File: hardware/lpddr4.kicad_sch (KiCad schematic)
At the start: 64 parts, among them IC11 K4F6E3S4HM-MGCJ, IC12 K4F6E3S4HM-MGCJ, U9 MPFS025T-FCVG484E

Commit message: assigned footprints of resistors and some capacitors
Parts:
- C101, C126, C127, C150, C151: value C -> 10uF; footprint (none) -> payload_footprints:CAPC1608X100N
- R105: value R_US -> 240R; footprint (none) -> payload_footprints:RESC1005X40N
- R106: value R_US -> 10K; footprint (none) -> payload_footprints:RC0402N_YAG
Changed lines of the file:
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@@
 			)
 		)
-		(property "Value" "C"
+		(property "Value" "10uF"
 			(at 202.946 266.446 0)
 			(show_name no)
@@
 			)
 		)
-		(property "Footprint" ""
+		(property "Footprint" "payload_footprints:CAPC1608X100N"
 			(at 200.9648 260.35 0)
 			(hide yes)
@@
 			)
 		)
-		(property "Value" "R_US"
+		(property "Value" "10K"
 			(at 255.905 181.6099 0)
 			(show_name no)
@@
 			)
 		)
-		(property "Footprint" ""
+		(property "Footprint" "payload_footprints:RC0402N_YAG"
 			(at 252.984 180.086 90)
 			(hide yes)
@@
 			)
 		)
-		(property "Value" "R_US"
+		(property "Value" "240R"
 			(at 265.43 158.242 90)
 			(show_name no)
@@
 			)
 		)
-		(property "Footprint" ""
+		(property "Footprint" "payload_footprints:RESC1005X40N"
 			(at 259.334 159.004 90)
 			(hide yes)
@@
 			)
 		)
-		(property "Value" "C"
+		(property "Value" "10uF"
 			(at 210.566 235.966 0)
 			(show_name no)
@@
 			)
 		)
-		(property "Footprint" ""
+		(property "Footprint" "payload_footprints:CAPC1608X100N"
 			(at 208.5848 229.87 0)
 			(hide yes)
@@
 			)
 		)
-		(property "Value" "C"
+		(property "Value" "10uF"
 			(at 195.326 266.446 0)
 			(show_name no)
@@
 			)
 		)
-		(property "Footprint" ""
+		(property "Footprint" "payload_footprints:CAPC1608X100N"
 			(at 193.3448 260.35 0)
 			(hide yes)
@@
 			)
 		)
-		(property "Value" "C"
+		(property "Value" "10uF"
 			(at 216.916 206.756 0)
 			(show_name no)
@@
 			)
 		)
-		(property "Footprint" ""
+		(property "Footprint" "payload_footprints:CAPC1608X100N"
 			(at 214.9348 200.66 0)
 			(hide yes)
@@
 			)
 		)
-		(property "Value" "C"
+		(property "Value" "10uF"
 			(at 218.186 235.966 0)
 			(show_name no)
@@
 			)
 		)
-		(property "Footprint" ""
+		(property "Footprint" "payload_footprints:CAPC1608X100N"
 			(at 216.2048 229.87 0)
 			(hide yes)

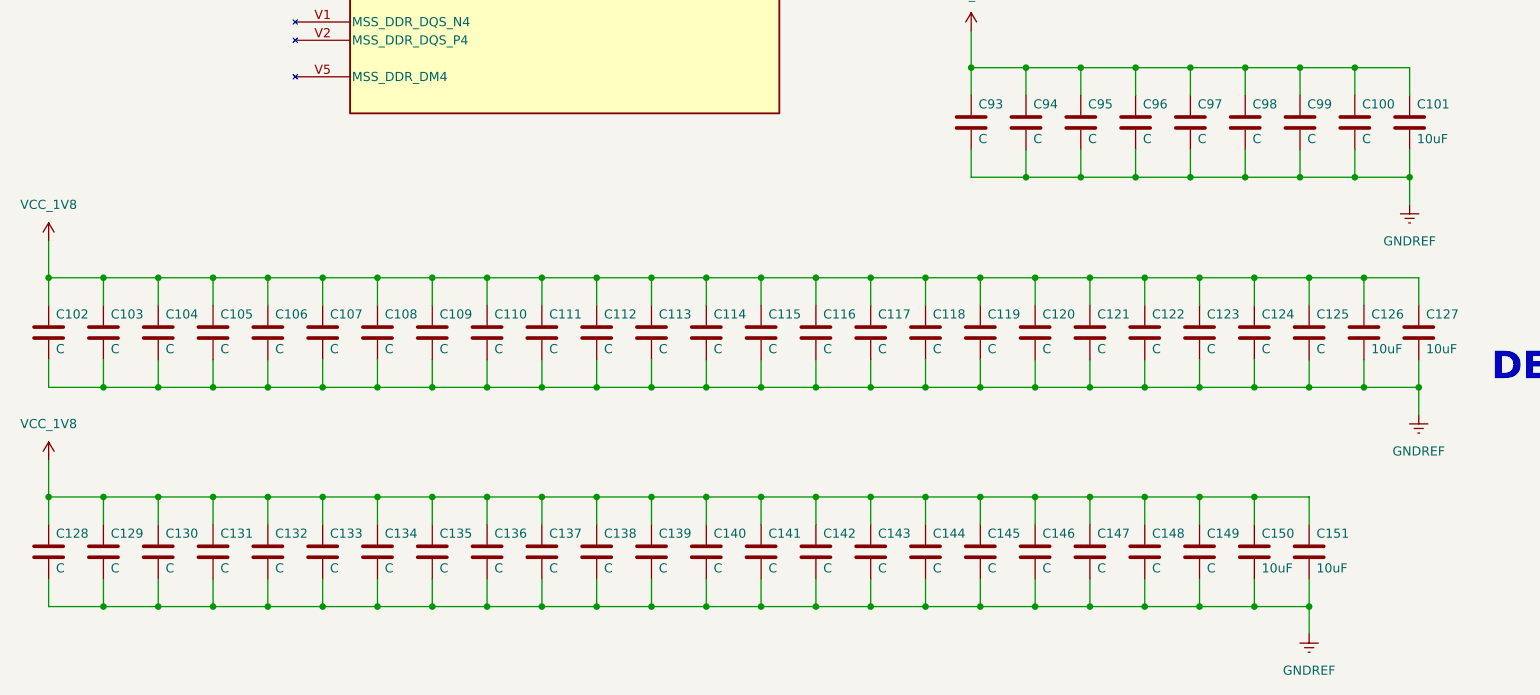
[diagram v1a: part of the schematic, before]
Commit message: added capacitors footprints
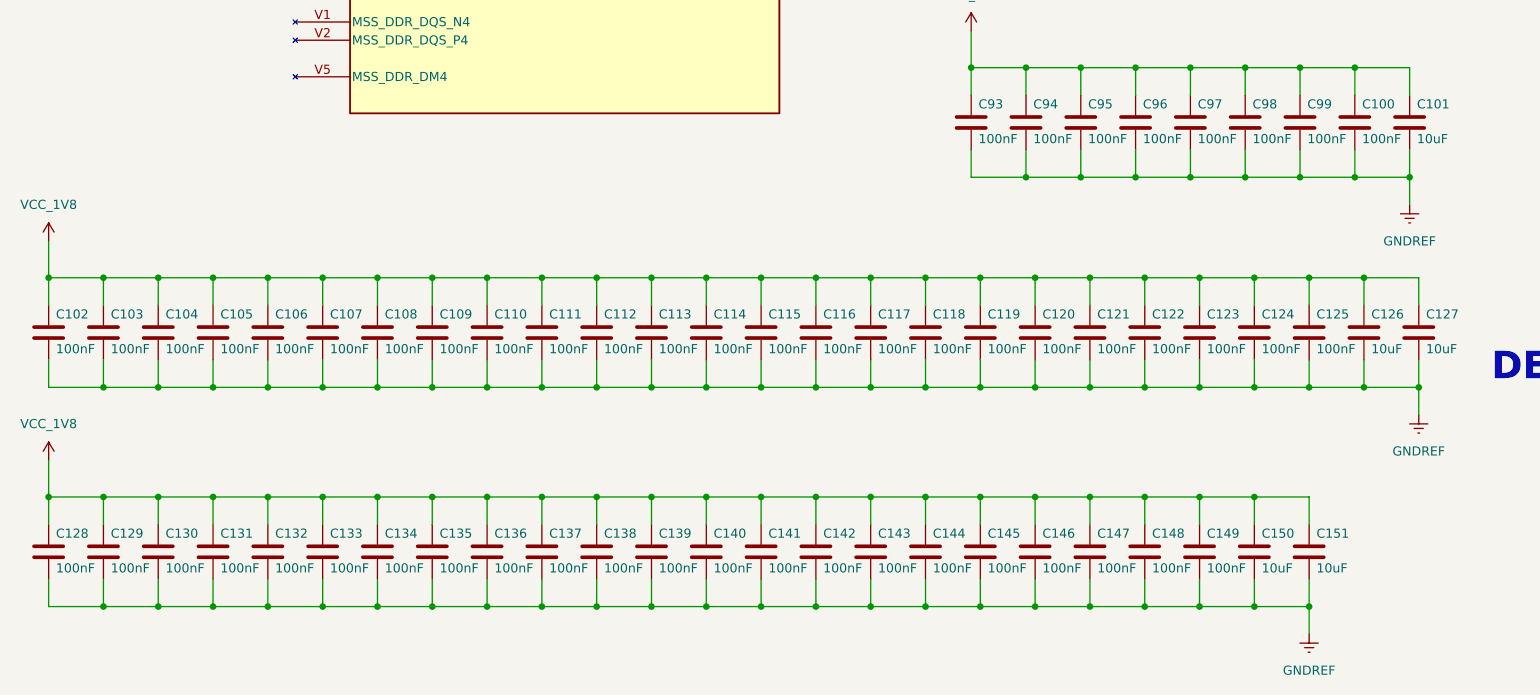
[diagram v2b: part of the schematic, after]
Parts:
- C100, C102, C103, C104, C105, C106, C107, C108, C109, C110, C111, C112, C113, C114, C115, C116, C117, C118, C119, C120, C121, C122, C123, C124, C125, C128, C129, C130, C131, C132, C133, C134, C135, C136, C137, C138, C139, C140, C141, C142, C143, C144, C145, C146, C147, C148, C149, C93, C94, C95, C96, C97, C98, C99: value C -> 100nF; footprint (none) -> payload_footprints:CAPC0603X35N
